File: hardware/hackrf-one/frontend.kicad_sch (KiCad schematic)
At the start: 143 parts, among them J2 RF-SHIELD-FRAME, J3 RF-SHIELD-COVER, J4 MOUNTING_HOLE, J5 MOUNTING_HOLE, J6 MOUNTING_HOLE, J7 MOUNTING_HOLE, J8 MOUNTING_HOLE, J9 MOUNTING_HOLE, P13 GPO1, P19 GPO3, P27 MIXER_SDATA, P31 MIXER_SCLK, P32 MIXER_ENX, P33 MIXER_RESETX, P34 MIX_BYPASS, P35 !MIX_BYPASS, P4 ANTENNA, P43 RX, P44 HP, P45 LP, P46 TX_MIX_BP, P47 RX_MIX_BP, P48 TX_AMP, P49 RX_AMP, P50 AMP_BYPASS, P51 !TX_AMP_PWR, P52 !RX_AMP_PWR, P6 GPO4, Q1 MOSFET_P, Q2 MOSFET_P, Q4 MOSFET_P, T1 MIX_IN_BALUN, T2 MIX_OUT_BALUN, U1 SKY13453, U10 SKY13453, U11 SKY13453, U12 SKY13317, U13 MGA-81563, U14 SKY13317, U2 SKY13453, U25 MGA-81563, U3 LOWPASS_FILTER, U4 RFFC5072, U5 SKY13453, U6 SKY13453, U7 SKY13453, U8 HIGHPASS_FILTER, U9 SKY13317

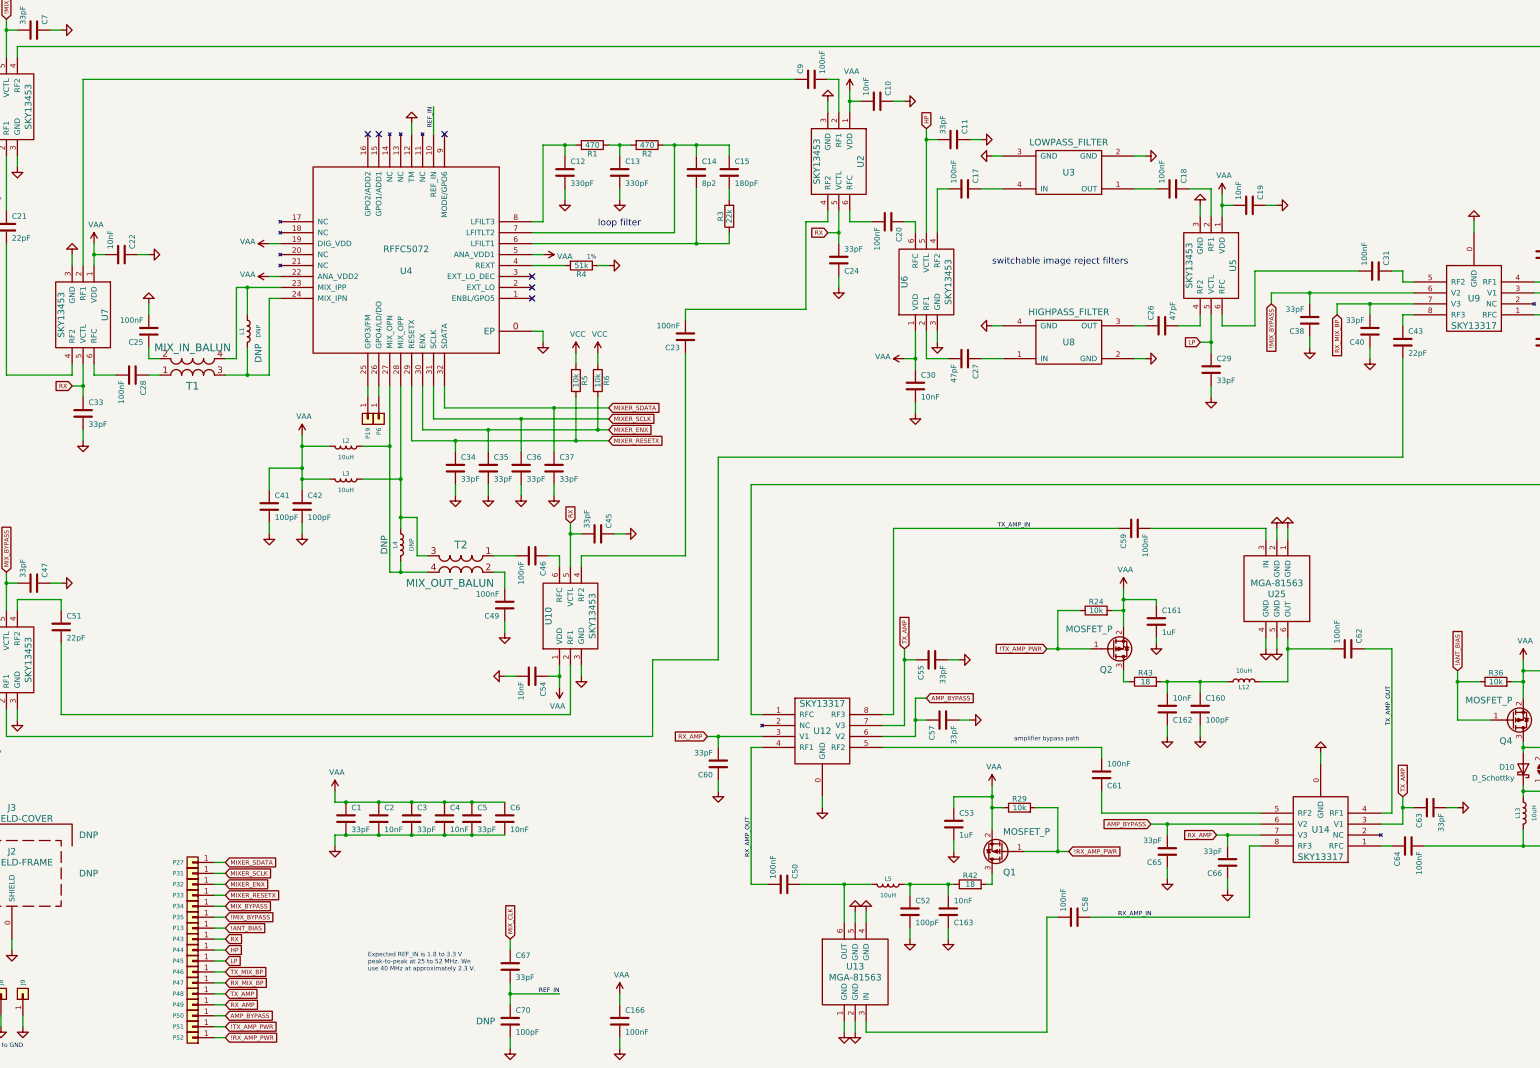
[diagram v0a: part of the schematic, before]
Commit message: HackRF One: revert hardware design to 8727449
This commit is between r8 and r9 and will be used as the basis for r10.
It includes some of the changes in r9 but predates the major changes to
the clock generator and IF transceiver ICs.
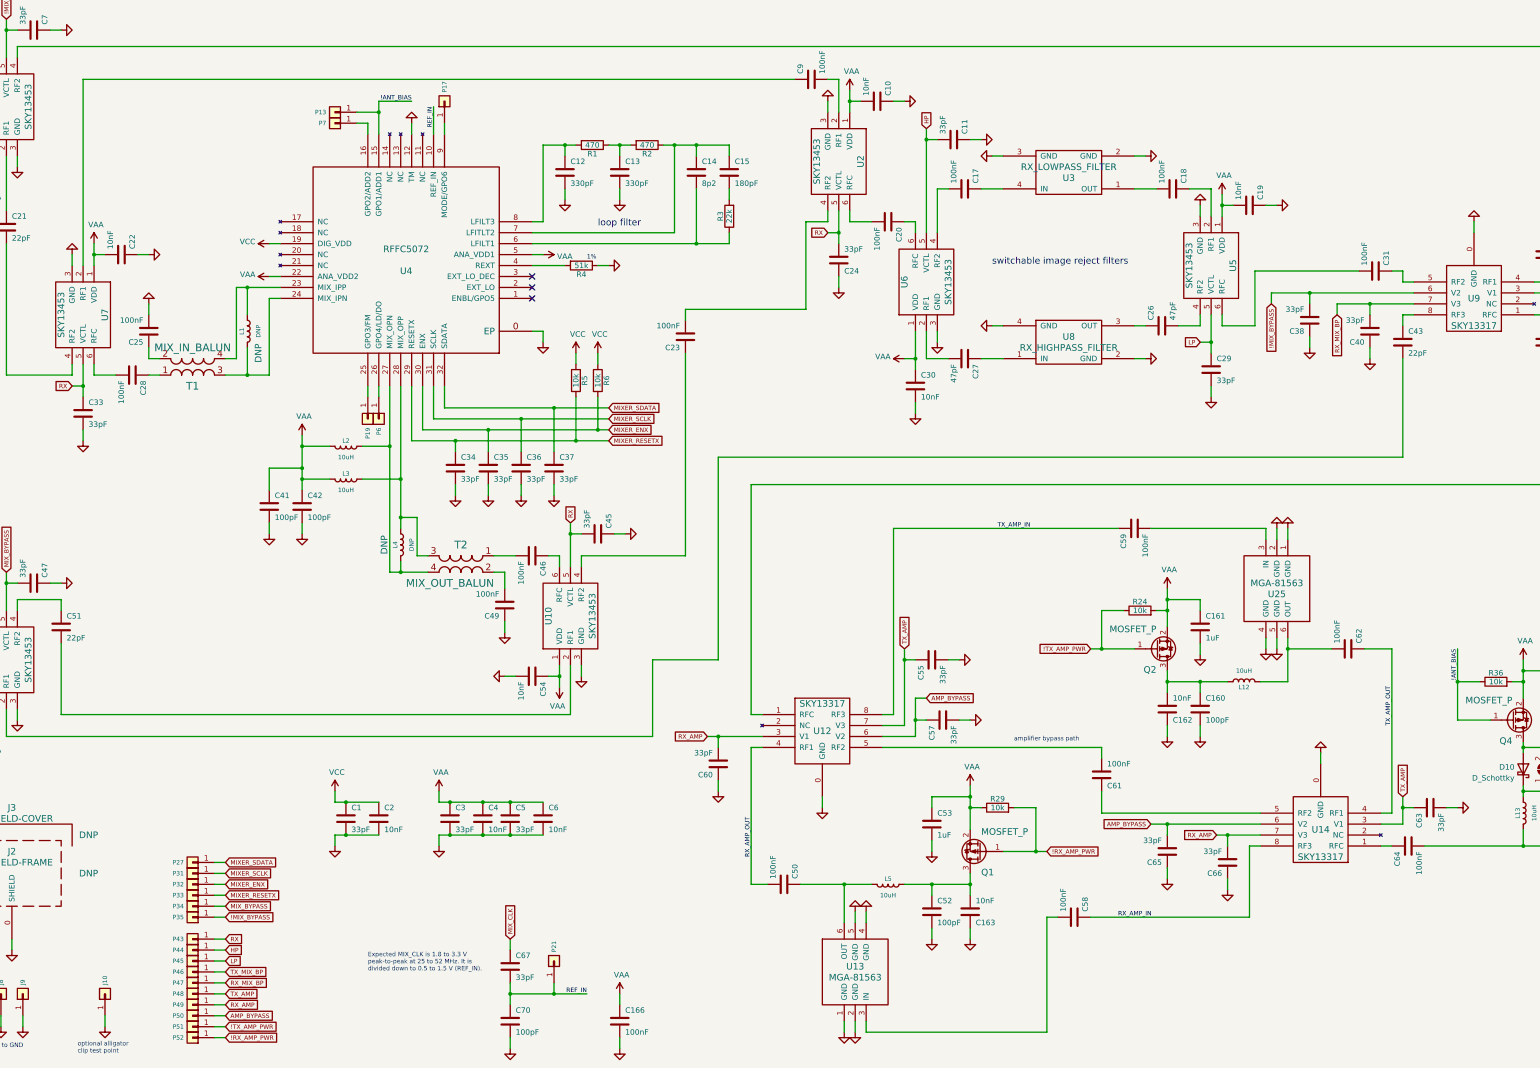
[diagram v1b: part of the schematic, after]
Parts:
- removed R42, R43: 18, hackrf:GSG-0402, symbol Device:R
- added J10: GND_CLIP, hackrf:GSG-TEST-POINT-S1751-46R, symbol Connector_Generic:Conn_01x01
- added P17: GPO6, hackrf:GSG-TESTPOINT-50MIL, symbol Connector_Generic:Conn_01x01
- added P21: REF_IN, hackrf:GSG-TESTPOINT-50MIL, symbol Connector_Generic:Conn_01x01
- added P7: GPO2, hackrf:GSG-TESTPOINT-50MIL, symbol Connector_Generic:Conn_01x01
- C1, C11, C24, C29, C3, C33, C34, C35, C36, C37, C38, C39, C40, C45, C47, C5, C55, C57, C60, C63, C65, C66, C67, C7: Manufacturer Samsung -> Murata; Part Number CL05C330JB5NNNC -> GRM1555C1H330JA01D
- C10, C16, C162, C163, C19, C2, C22, C30, C4, C54, C56, C6: Manufacturer Samsung -> Murata; Part Number CL05B103KB5NNNC -> GRM155R71C103KA01D
- C12, C13: Manufacturer Samsung -> Murata; Part Number CL05C331JB5NNNC -> GRM155R71H331KA01D
- C14: Manufacturer Yageo -> Taiyo Yuden; Part Number CC0402CRNPO9BN8R2 -> UMK105CG8R2DV-F
- C15: Manufacturer Yageo -> Murata; Part Number CC0402JRNPO9BN181 -> GRM1555C1H181JA01D
- C160, C41, C42, C52: Manufacturer Samsung -> Murata; Part Number CL05C101JB5NNNC -> GRM1555C1H101JA01D
- C161, C171, C53: Manufacturer Samsung -> Taiyo Yuden; Part Number CL05A105KP5NNNC -> LMK105BJ105KV-F
- C166, C17, C18, C20, C23, C25, C28, C31, C44, C46, C49, C50, C58, C59, C61, C62, C64, C9: Manufacturer Samsung -> Murata; Part Number CL05A104KA5NNNC -> GRM155R61A104KA01D
- C21, C32, C43, C48, C51, C8: Manufacturer Samsung -> Murata; Part Number CL05C220JB5NNNC -> GRM1555C1H220JA01D
- C26, C27: Manufacturer Samsung -> Murata; Part Number CL05C470JB5NNNC -> GRM1555C1H470JA01D
- C70: DNP DNP -> (none); Manufacturer Samsung -> Murata; Part Number CL05C101JB5NNNC -> GRM1555C1H101JA01D
- J2, J3, J4, J5, J6, J7, J8, J9, L1, L4, P13, P19, P27, P31, P32, P33, P34, P35, P43, P44, P45, P46, P47, P48, P49, P50, P51, P52, P6: DNP DNP -> (none); Note (none) -> DNP
- JP1: DNP DNP -> (none)
- Q1, Q2, Q4: Manufacturer Yangzhou Yangjie -> Fairchild; Part Number YJL2301C -> BSS84
- U3: value LOWPASS_FILTER -> RX_LOWPASS_FILTER
- U8: value HIGHPASS_FILTER -> RX_HIGHPASS_FILTER
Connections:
- net !ANT_BIAS: now also U4.15 (GPO1/ADD1)
- net GND: now also J10.1 (Pin_1)
- net REF_IN: now also P21.1 (Pin_1)
- net VAA: no longer C1.1, C2.1, U4.19 (DIG_VDD)
- net VCC: now also C1.1, C2.1, U4.19 (DIG_VDD)
- net at U4.16 (GPO2/ADD2): now also P7.1 (Pin_1)
- net at U4.9 (MODE/GPO6): now also P17.1 (Pin_1)
- net at C163.2, C52.1, L5.1: now also Q1.3 (D)
- net at C160.1, C162.2, L12.1: now also Q2.3 (D)
- no-connect marks 6 -> 3
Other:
- note added: "Expected MIX_CLK is 1.8 to 3.3 V peak-to-peak at 25 to 52 MHz. It is divided down to 0.5 to 1.5 V (REF_IN)."
- note added: "optional alligator clip test point"
- note removed: "Expected REF_IN is 1.8 to 3.3 V peak-to-peak at 25 to 52 MHz. We use 40 MHz at approximately 2.3 V."
- moved on the sheet: C161, C163, C3, C4, C5, C52, C53, C6, P13, Q1, Q2, R24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

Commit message: HackRF One: update version to 8+
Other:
- company: Copyright 2012-2022 Great Scott Gadgets -> ${COPYRIGHT}
- title: HackRF One -> ${TITLE}
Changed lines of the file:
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@@
   (paper "User" 431.8 279.4)
   (title_block
-    (title "HackRF One")
-    (date "2022-08-28")
-    (rev "r9")
-    (company "Copyright 2012-2022 Great Scott Gadgets")
-    (comment 1 "Michael Ossmann")
-    (comment 2 "Licensed under the CERN-OHL-P v2")
+    (title "${TITLE}")
+    (date "${DATE}")
+    (rev "${VERSION}")
+    (company "${COPYRIGHT}")
+    (comment 1 "${LICENSE}")
   )
   (junction (at 111.76 121.92) (diameter 0) (color 0 0 0 0)

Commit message: HackRF One: use DNP field instead of Note field
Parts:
- J10, J2, J3, J4, J5, J6, J7, J8, J9, L1, L4, P13, P17, P19, P21, P27, P31, P32, P33, P34, P35, P43, P44, P45, P46, P47, P48, P49, P50, P51, P52, P6, P7: DNP (none) -> DNP; Note DNP -> (none)
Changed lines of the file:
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@@
       (effects (font (size 1.524 1.524)) hide)
     )
-    (property "Note" "DNP" (id 4) (at 130.81 144.78 90)
+    (property "DNP" "DNP" (id 4) (at 130.81 144.78 90)
       (effects (font (size 1.524 1.524)))
     )
@@
       (effects (font (size 1.524 1.524)) hide)
     )
-    (property "Note" "DNP" (id 4) (at 101.6 100.33 90)
+    (property "DNP" "DNP" (id 4) (at 101.6 100.33 90)
       (effects (font (size 1.524 1.524)))
     )
@@
       (effects (font (size 1.524 1.524)) hide)
     )
-    (property "Note" "DNP" (id 4) (at 129.54 115.57 0)
+    (property "DNP" "DNP" (id 4) (at 129.54 115.57 0)
       (effects (font (size 1.524 1.524)) hide)
     )
@@
       (effects (font (size 1.524 1.524)) hide)
     )
-    (property "Note" "DNP" (id 7) (at 62.23 220.98 0)
+    (property "DNP" "DNP" (id 7) (at 62.23 220.98 0)
       (effects (font (size 1.524 1.524)))
     )
@@
       (effects (font (size 1.524 1.524)) hide)
     )
-    (property "Note" "DNP" (id 7) (at 62.23 212.09 0)
+    (property "DNP" "DNP" (id 7) (at 62.23 212.09 0)
       (effects (font (size 1.524 1.524)))
     )
@@
       (effects (font (size 1.524 1.524)) hide)
     )
-    (property "Note" "DNP" (id 4) (at 127 115.57 0)
+    (property "DNP" "DNP" (id 4) (at 127 115.57 0)
       (effects (font (size 1.524 1.524)) hide)
     )
@@
       (effects (font (size 1.524 1.524)) hide)
     )
-    (property "Note" "DNP" (id 4) (at 119.38 46.99 0)
+    (property "DNP" "DNP" (id 4) (at 119.38 46.99 0)
       (effects (font (size 1.524 1.524)) hide)
     )
@@
       (effects (font (size 1.524 1.524)) hide)
     )
-    (property "Note" "DNP" (id 4) (at 119.38 44.45 0)
+    (property "DNP" "DNP" (id 4) (at 119.38 44.45 0)
       (effects (font (size 1.524 1.524)) hide)
     )
@@
       (effects (font (size 1.524 1.524)) hide)
     )
-    (property "Note" "DNP" (id 4) (at 170.18 241.3 0)
+    (property "DNP" "DNP" (id 4) (at 170.18 241.3 0)
       (effects (font (size 1.524 1.524)) hide)
     )
@@
       (effects (font (size 1.524 1.524)) hide)
     )
-    (property "Note" "DNP" (id 4) (at 144.78 41.91 0)
+    (property "DNP" "DNP" (id 4) (at 144.78 41.91 0)
       (effects (font (size 1.524 1.524)) hide)
     )
@@
       (effects (font (size 1.524 1.524)) hide)
     )
-    (property "Note" "DNP" (id 4) (at 86.36 218.44 0)
+    (property "DNP" "DNP" (id 4) (at 86.36 218.44 0)
       (effects (font (size 1.524 1.524)) hide)
     )
@@
       (effects (font (size 1.524 1.524)) hide)
     )
-    (property "Note" "DNP" (id 4) (at 86.36 220.98 0)
+    (property "DNP" "DNP" (id 4) (at 86.36 220.98 0)
       (effects (font (size 1.524 1.524)) hide)
     )
@@
       (effects (font (size 1.524 1.524)) hide)
     )
-    (property "Note" "DNP" (id 4) (at 86.36 223.52 0)
+    (property "DNP" "DNP" (id 4) (at 86.36 223.52 0)
       (effects (font (size 1.524 1.524)) hide)
     )
@@
       (effects (font (size 1.524 1.524)) hide)
     )
-    (property "Note" "DNP" (id 4) (at 86.36 226.06 0)
+    (property "DNP" "DNP" (id 4) (at 86.36 226.06 0)
       (effects (font (size 1.524 1.524)) hide)
     )
@@
       (effects (font (size 1.524 1.524)) hide)
     )
-    (property "Note" "DNP" (id 4) (at 86.36 228.6 0)
+    (property "DNP" "DNP" (id 4) (at 86.36 228.6 0)
       (effects (font (size 1.524 1.524)) hide)
     )
@@
       (effects (font (size 1.524 1.524)) hide)
     )
-    (property "Note" "DNP" (id 4) (at 86.36 231.14 0)
+    (property "DNP" "DNP" (id 4) (at 86.36 231.14 0)
       (effects (font (size 1.524 1.524)) hide)
     )
@@
       (effects (font (size 1.524 1.524)) hide)
     )
-    (property "Note" "DNP" (id 4) (at 86.36 236.22 0)
+    (property "DNP" "DNP" (id 4) (at 86.36 236.22 0)
       (effects (font (size 1.524 1.524)) hide)
     )
@@
       (effects (font (size 1.524 1.524)) hide)
     )
-    (property "Note" "DNP" (id 4) (at 86.36 238.76 0)
+    (property "DNP" "DNP" (id 4) (at 86.36 238.76 0)
       (effects (font (size 1.524 1.524)) hide)
     )
@@
       (effects (font (size 1.524 1.524)) hide)
     )
-    (property "Note" "DNP" (id 4) (at 86.36 241.3 0)
+    (property "DNP" "DNP" (id 4) (at 86.36 241.3 0)
       (effects (font (size 1.524 1.524)) hide)
     )
@@
       (effects (font (size 1.524 1.524)) hide)
     )
-    (property "Note" "DNP" (id 4) (at 86.36 243.84 0)
+    (property "DNP" "DNP" (id 4) (at 86.36 243.84 0)
       (effects (font (size 1.524 1.524)) hide)
     )
@@
       (effects (font (size 1.524 1.524)) hide)
     )
-    (property "Note" "DNP" (id 4) (at 86.36 246.38 0)
+    (property "DNP" "DNP" (id 4) (at 86.36 246.38 0)
       (effects (font (size 1.524 1.524)) hide)
     )
@@
       (effects (font (size 1.524 1.524)) hide)
     )
-    (property "Note" "DNP" (id 4) (at 86.36 248.92 0)
+    (property "DNP" "DNP" (id 4) (at 86.36 248.92 0)
       (effects (font (size 1.524 1.524)) hide)
     )
@@
       (effects (font (size 1.524 1.524)) hide)
     )
-    (property "Note" "DNP" (id 4) (at 86.36 251.46 0)
+    (property "DNP" "DNP" (id 4) (at 86.36 251.46 0)
       (effects (font (size 1.524 1.524)) hide)
     )
@@
       (effects (font (size 1.524 1.524)) hide)
     )
-    (property "Note" "DNP" (id 4) (at 86.36 254 0)
+    (property "DNP" "DNP" (id 4) (at 86.36 254 0)
       (effects (font (size 1.524 1.524)) hide)
     )
@@
       (effects (font (size 1.524 1.524)) hide)
     )
-    (property "Note" "DNP" (id 4) (at 86.36 256.54 0)
+    (property "DNP" "DNP" (id 4) (at 86.36 256.54 0)
       (effects (font (size 1.524 1.524)) hide)
     )
@@
       (effects (font (size 1.524 1.524)) hide)
     )
-    (property "Note" "DNP" (id 4) (at 86.36 259.08 0)
+    (property "DNP" "DNP" (id 4) (at 86.36 259.08 0)
       (effects (font (size 1.524 1.524)) hide)
     )
@@
       (effects (font (size 1.524 1.524)) hide)
     )
-    (property "Note" "DNP" (id 4) (at 21.59 248.92 0)
+    (property "DNP" "DNP" (id 4) (at 21.59 248.92 0)
       (effects (font (size 1.524 1.524)) hide)
     )
@@
       (effects (font (size 1.524 1.524)) hide)
     )
-    (property "Note" "DNP" (id 4) (at 26.67 248.92 0)
+    (property "DNP" "DNP" (id 4) (at 26.67 248.92 0)
       (effects (font (size 1.524 1.524)) hide)
     )
@@
       (effects (font (size 1.524 1.524)) hide)
     )
-    (property "Note" "DNP" (id 4) (at 31.75 248.92 0)
+    (property "DNP" "DNP" (id 4) (at 31.75 248.92 0)
       (effects (font (size 1.524 1.524)) hide)
     )
@@
       (effects (font (size 1.524 1.524)) hide)
     )
-    (property "Note" "DNP" (id 4) (at 36.83 248.92 0)
+    (property "DNP" "DNP" (id 4) (at 36.83 248.92 0)
       (effects (font (size 1.524 1.524)) hide)
     )
@@
       (effects (font (size 1.524 1.524)) hide)
     )
-    (property "Note" "DNP" (id 4) (at 41.91 248.92 0)
+    (property "DNP" "DNP" (id 4) (at 41.91 248.92 0)
       (effects (font (size 1.524 1.524)) hide)
     )
@@
       (effects (font (size 1.524 1.524)) hide)
     )
-    (property "Note" "DNP" (id 4) (at 46.99 248.92 0)
+    (property "DNP" "DNP" (id 4) (at 46.99 248.92 0)
       (effects (font (size 1.524 1.524)) hide)
     )
@@
       (effects (font (size 1.524 1.524)) hide)
     )
-    (property "Note" "DNP" (id 7) (at 66.04 248.92 0)
+    (property "DNP" "DNP" (id 7) (at 66.04 248.92 0)
       (effects (font (size 1.524 1.524)) hide)
     )

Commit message: HackRF One: update component selections
Add Substitution field
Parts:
- C1, C11, C24, C29, C3, C33, C34, C35, C36, C37, C38, C39, C40, C45, C47, C5, C55, C57, C60, C63, C65, C66, C67, C7: Manufacturer Murata -> Samsung; Part Number GRM1555C1H330JA01D -> CL05C330JB5NNNC; Substitution (none) -> Murata GRM1555C1H330JA01D
- C10, C16, C162, C163, C19, C2, C22, C30, C4, C54, C56, C6: Manufacturer Murata -> Samsung; Part Number GRM155R71C103KA01D -> CL05B103KB5NNNC; Substitution (none) -> Murata GRM155R71C103KA01D
- C12, C13: Manufacturer Murata -> Samsung; Part Number GRM155R71H331KA01D -> CL05C331JB5NNNC; Substitution (none) -> Murata GRM155R71H331KA01D
- C14: Manufacturer Taiyo Yuden -> Yageo; Part Number UMK105CG8R2DV-F -> CC0402CRNPO9BN8R2; Substitution (none) -> Taiyo Yuden UMK105CG8R2DV-F
- C15: Manufacturer Murata -> Yageo; Part Number GRM1555C1H181JA01D -> CC0402JRNPO9BN181; Substitution (none) -> Murata GRM1555C1H181JA01D
- C160, C41, C42, C52, C70: Manufacturer Murata -> Samsung; Part Number GRM1555C1H101JA01D -> CL05C101JB5NNNC; Substitution (none) -> Murata GRM1555C1H101JA01D
- C161, C171, C53: Manufacturer Taiyo Yuden -> Samsung; Part Number LMK105BJ105KV-F -> CL05A105KP5NNNC; Substitution (none) -> Taiyo Yuden LMK105BJ105KV-F
- C21, C32, C43, C48, C51, C8: Manufacturer Murata -> Samsung; Part Number GRM1555C1H220JA01D -> CL05C220JB5NNNC; Substitution (none) -> Murata GRM1555C1H220JA01D
- C26, C27: Manufacturer Murata -> Samsung; Part Number GRM1555C1H470JA01D -> CL05C470JB5NNNC; Substitution (none) -> Murata GRM1555C1H470JA01D
- Q1, Q2, Q4: Manufacturer Fairchild -> Yangzhou Yangjie; Part Number BSS84 -> YJL2301C
- R1, R2, R24, R29, R3, R36, R4, R5, R6: Substitution (none) -> any equivalent
- T1, T2: Manufacturer Anaren -> TTM
- U13, U25: Substitution (none) -> MGA-81563*
- U4: Substitution (none) -> RFFC5072*
